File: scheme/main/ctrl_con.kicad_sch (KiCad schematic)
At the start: 0 parts

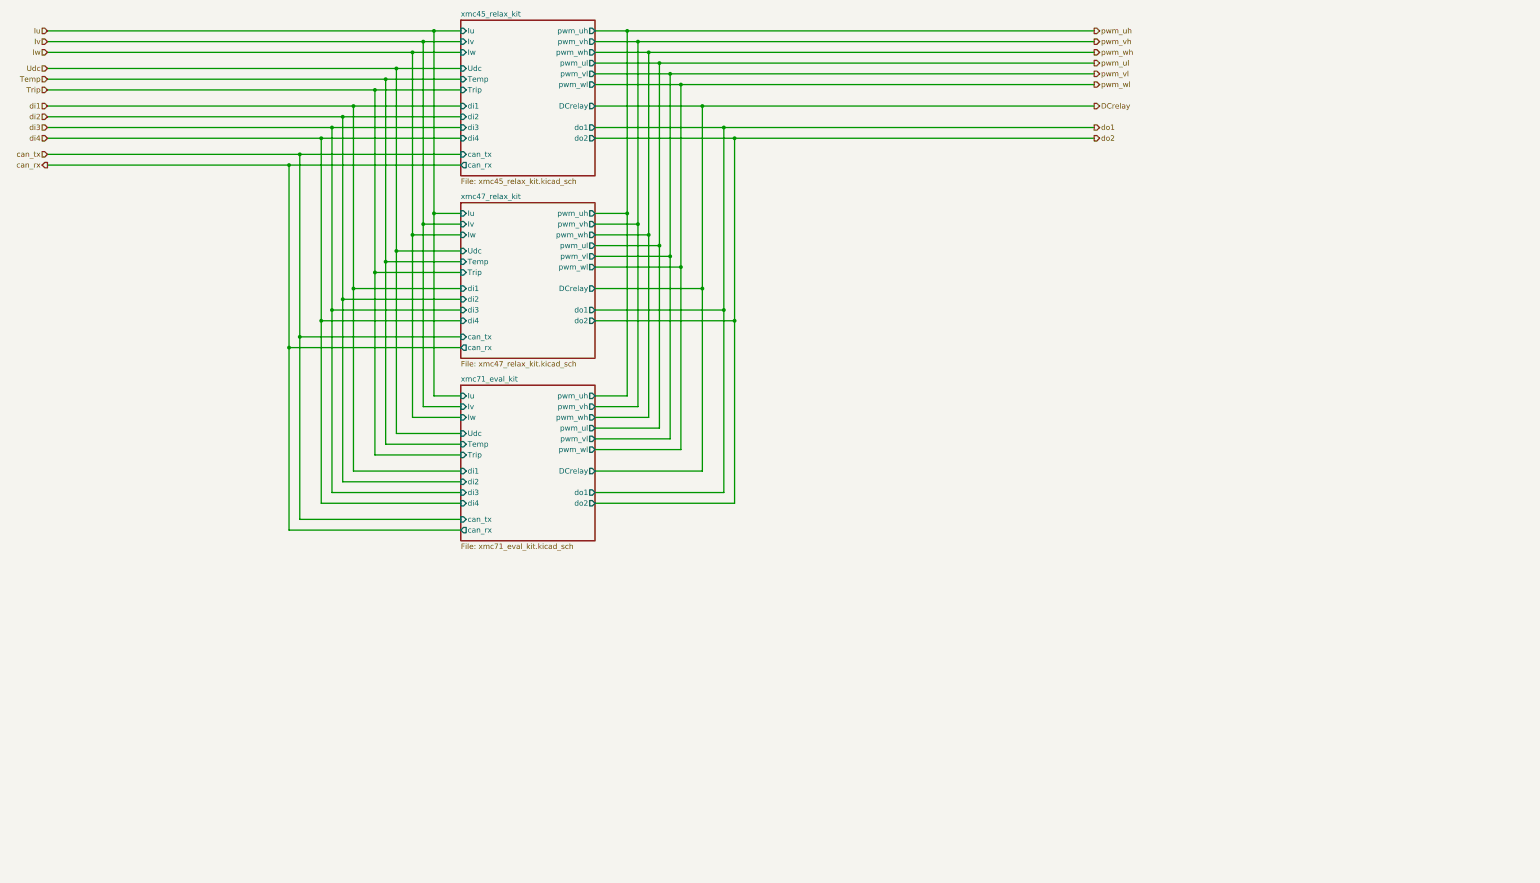
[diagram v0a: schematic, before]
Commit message: added adc driver & output buffer with oe
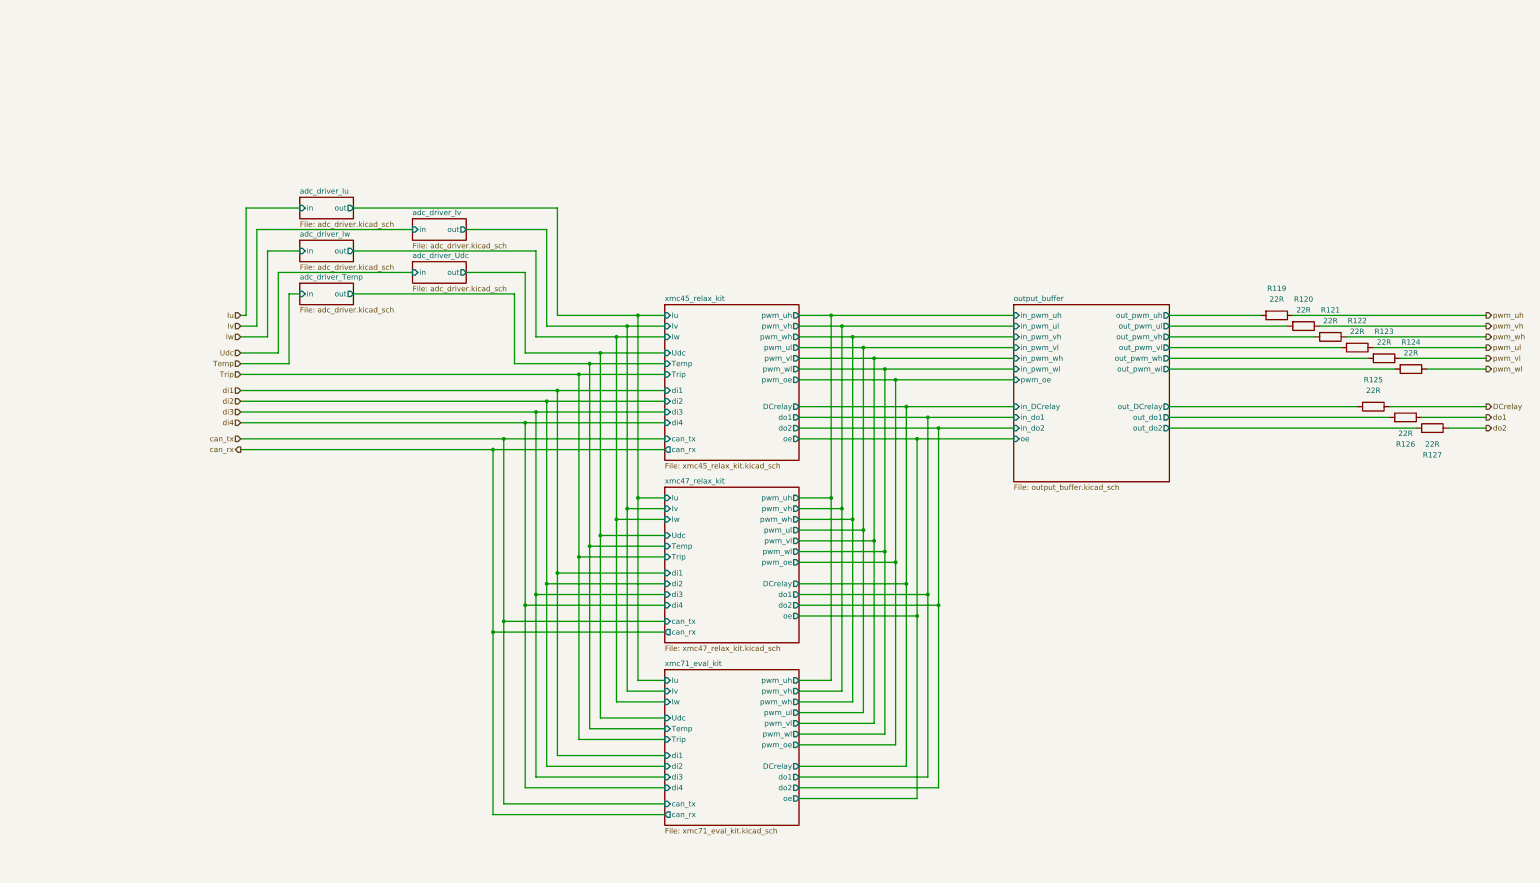
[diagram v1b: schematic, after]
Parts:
- added R119, R120, R121, R122, R123, R124, R125, R126, R127: 22R, Resistor_SMD:R_0805_2012Metric, symbol Device:R
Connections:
- net DCrelay: now also R125.1
- net do1: now also R126.1
- net do2: now also R127.1
- net pwm_uh: now also R119.1
- net pwm_ul: now also R122.1
- net pwm_vh: now also R120.1
- net pwm_vl: now also R123.1
- net pwm_wh: now also R121.1
- net pwm_wl: now also R124.1
- new net output_buffer/out_DCrelay: R125.2
- new net output_buffer/out_do1: R126.2
- new net output_buffer/out_do2: R127.2
- new net output_buffer/out_pwm_uh: R119.2
- new net output_buffer/out_pwm_ul: R120.2
- new net output_buffer/out_pwm_vh: R121.2
- new net output_buffer/out_pwm_vl: R122.2
- new net output_buffer/out_pwm_wh: R123.2
- new net output_buffer/out_pwm_wl: R124.2
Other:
- added sheet adc_driver_Iu (adc_driver.kicad_sch)
- added sheet adc_driver_Iv (adc_driver.kicad_sch)
- added sheet adc_driver_Iw (adc_driver.kicad_sch)
- added sheet adc_driver_Temp (adc_driver.kicad_sch)
- added sheet adc_driver_Udc (adc_driver.kicad_sch)
- added sheet output_buffer (output_buffer.kicad_sch)
- sheet xmc45_relax_kit ports: added oe, pwm_oe; removed none
- sheet xmc47_relax_kit ports: added oe, pwm_oe; removed none
- sheet xmc71_eval_kit ports: added oe, pwm_oe; removed none

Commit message: added input buffer
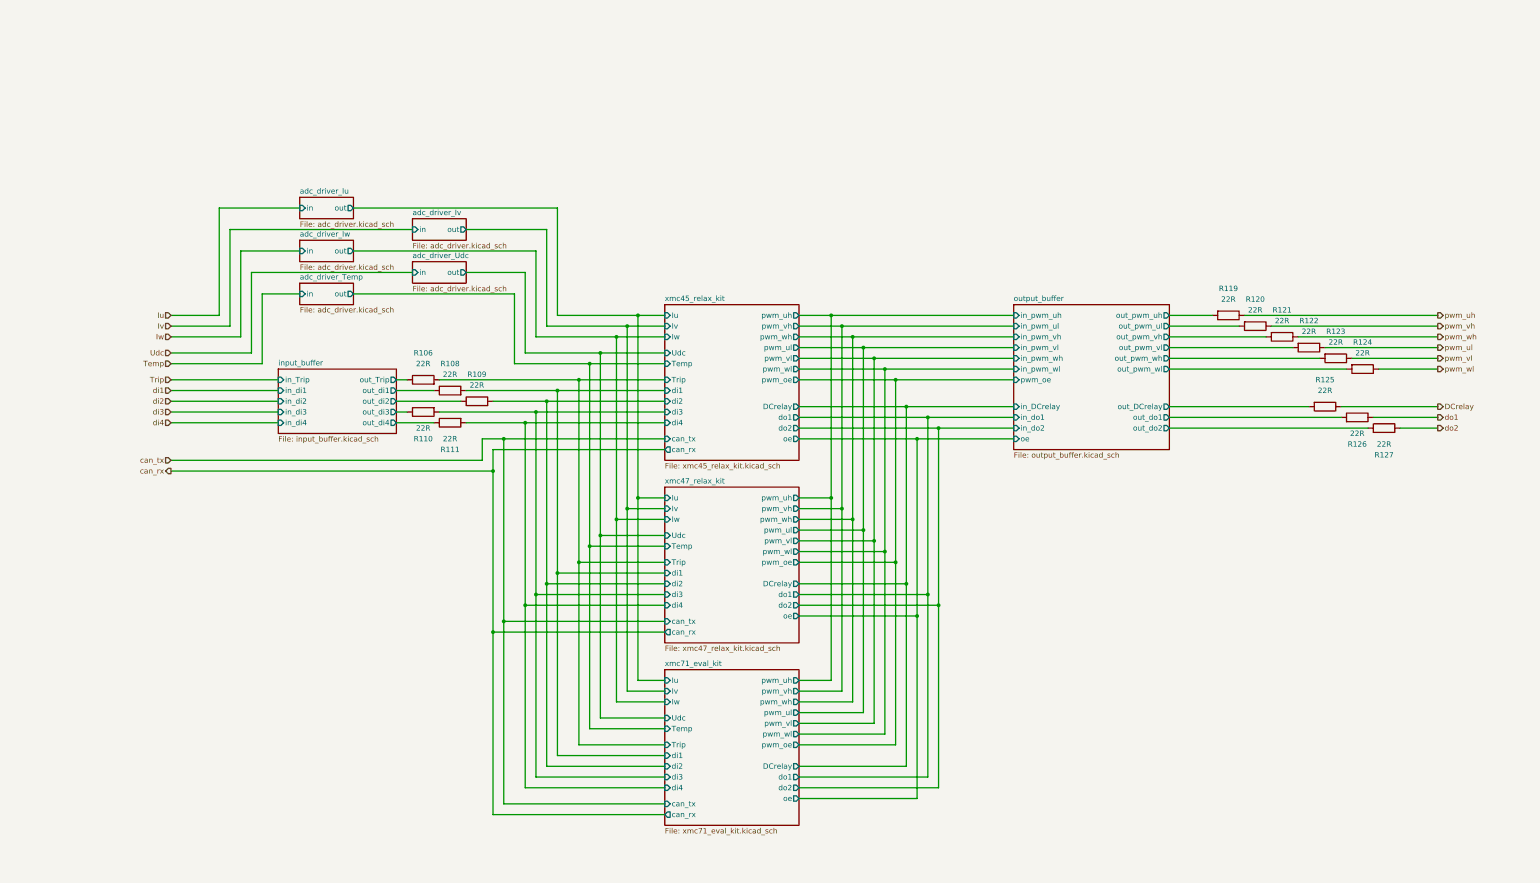
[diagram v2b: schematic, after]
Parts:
- added R106, R108, R109, R110, R111: 22R, Resistor_SMD:R_0805_2012Metric, symbol Device:R
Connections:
- new net input_buffer/out_Trip: R106.1
- new net input_buffer/out_di1: R108.1
- new net input_buffer/out_di2: R109.1
- new net input_buffer/out_di3: R110.1
- new net input_buffer/out_di4: R111.1
- new net xmc45_relax_kit/Trip: R106.2
- new net xmc45_relax_kit/di1: R108.2
- new net xmc45_relax_kit/di2: R109.2
- new net xmc45_relax_kit/di3: R110.2
- new net xmc45_relax_kit/di4: R111.2
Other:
- added sheet input_buffer (input_buffer.kicad_sch)
- moved on the sheet: R119, R120, R121, R122, R123, R124, R125, R126, R127

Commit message: sheets titles
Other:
- title: (none) -> Соединения с платами управления
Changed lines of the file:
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@@
 	(generator_version "8.0")
 	(paper "A3")
+	(title_block
+		(title "Соединения с платами управления")
+	)
 	(junction
 		(at 222.25 101.6)

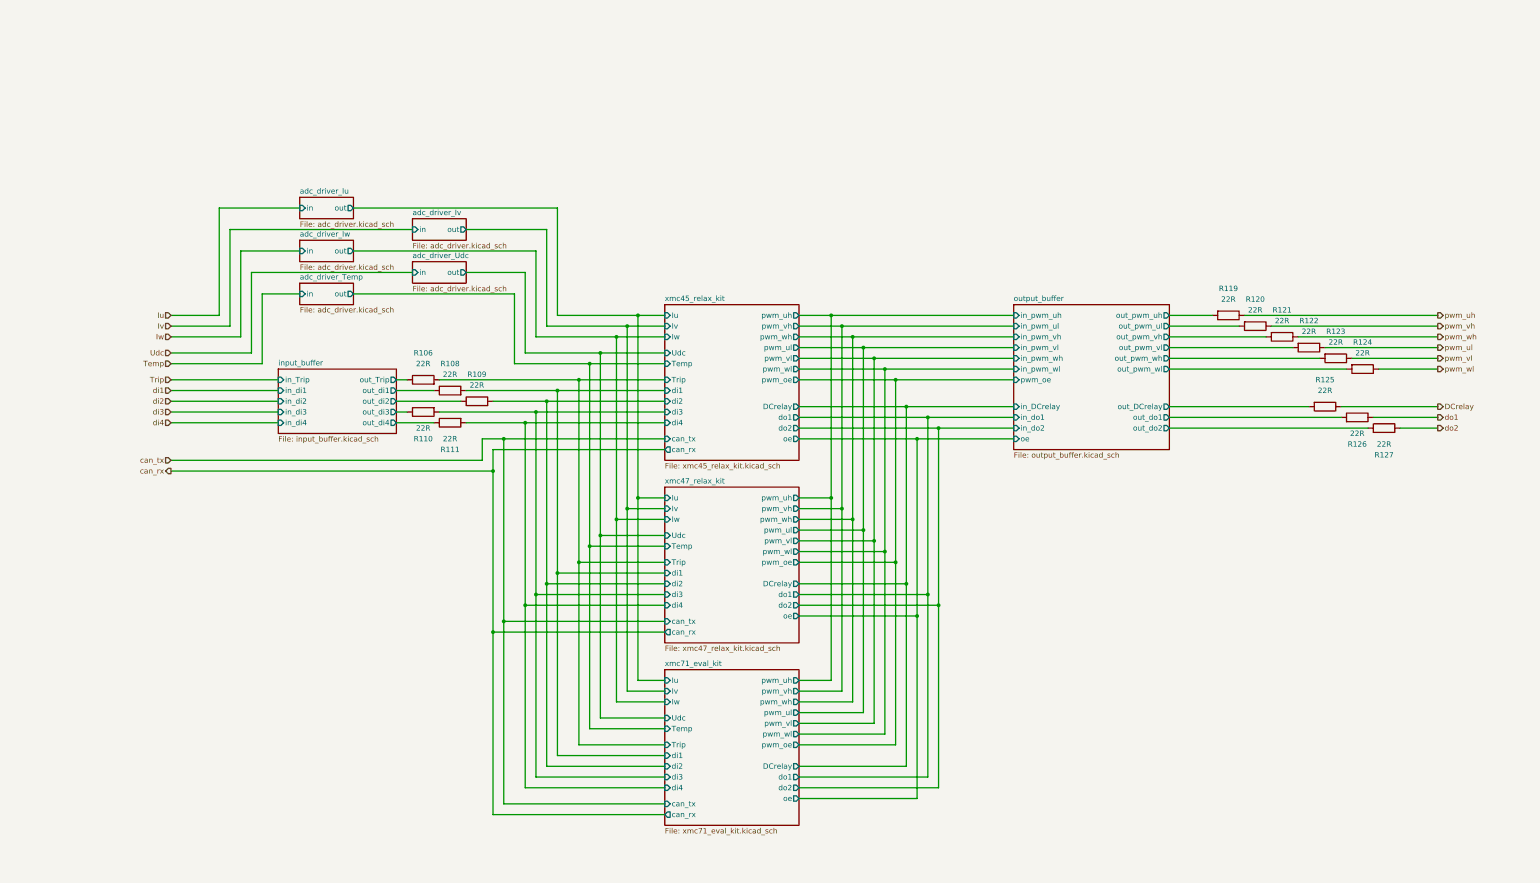
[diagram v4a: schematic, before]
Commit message: added analog input 0 && sheets sort
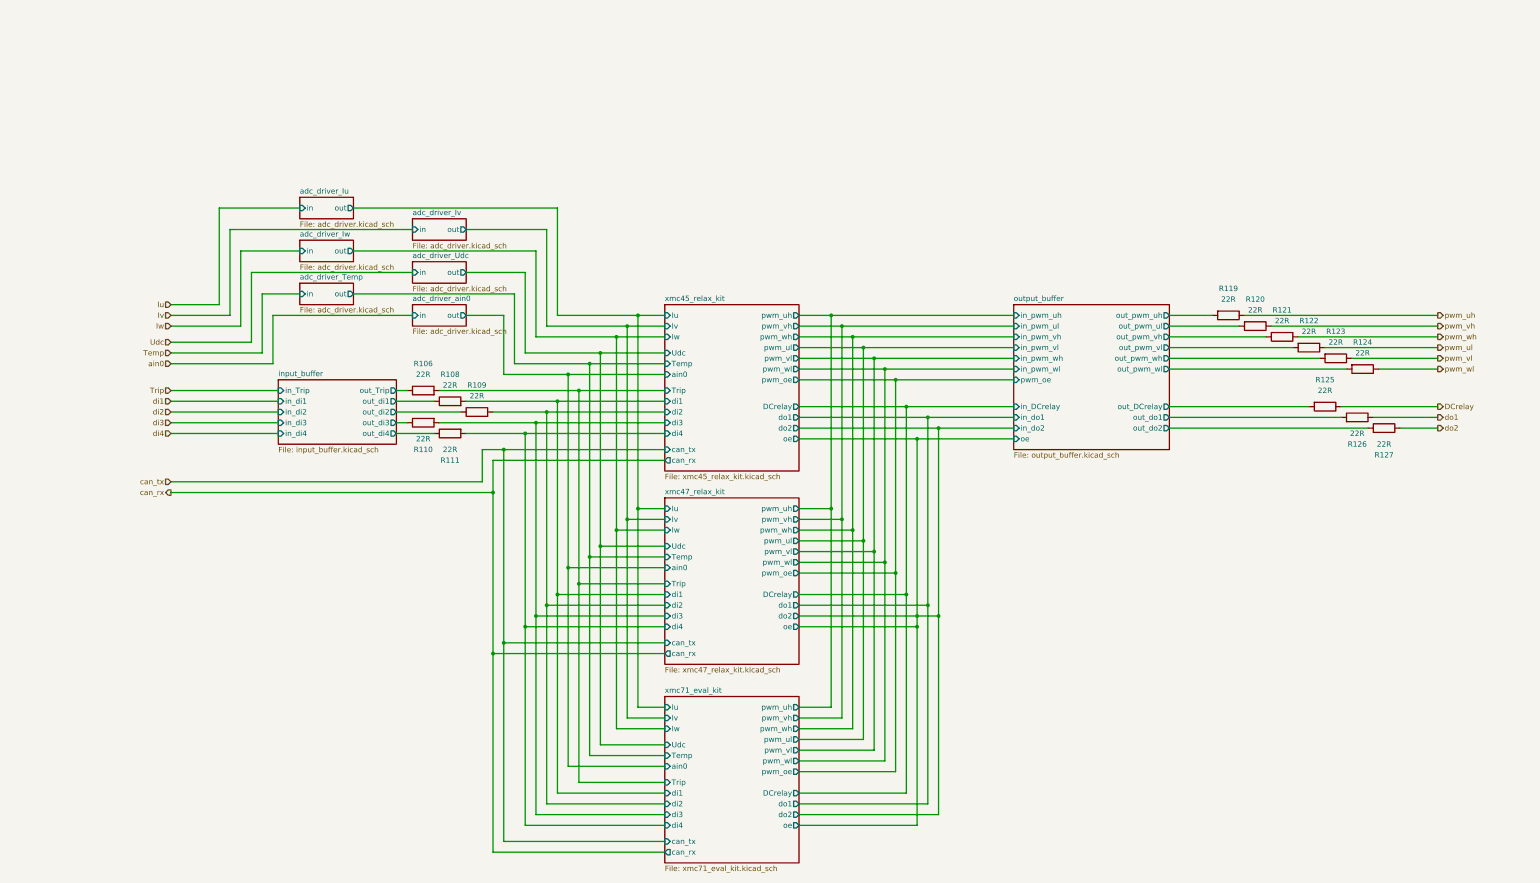
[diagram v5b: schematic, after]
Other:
- added sheet adc_driver_ain0 (adc_driver.kicad_sch)
- sheet xmc45_relax_kit ports: added ain0; removed none
- sheet xmc47_relax_kit ports: added ain0; removed none
- sheet xmc71_eval_kit ports: added ain0; removed none
- moved on the sheet: R106, R108, R109, R110, R111
